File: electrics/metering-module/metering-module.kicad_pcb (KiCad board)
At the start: 2 copper layers, 86 x 31 mm, 39 parts, among them J1 North, J2 South, J3 West, J4 East, Q1 MMBT3904, Q2 MMBT3904, U1 LTV-817S, U2 LTV-817S, U3 BA033CC0FP-E2, U4 MAX3486, U5 MAX3486, U6 MCP23009-E_SS

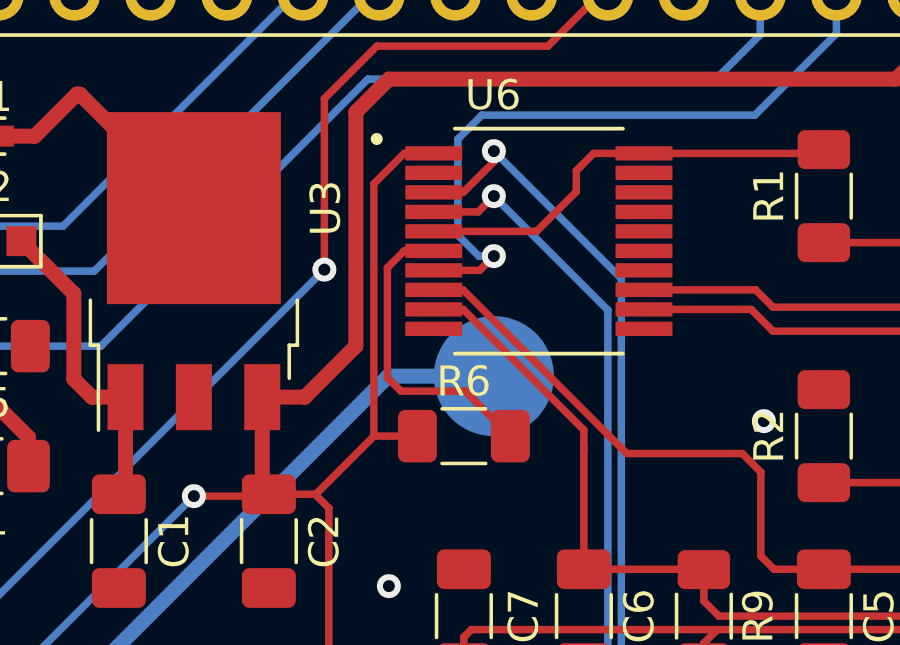
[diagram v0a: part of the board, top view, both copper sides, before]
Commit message: Added product numbers for cost calculation
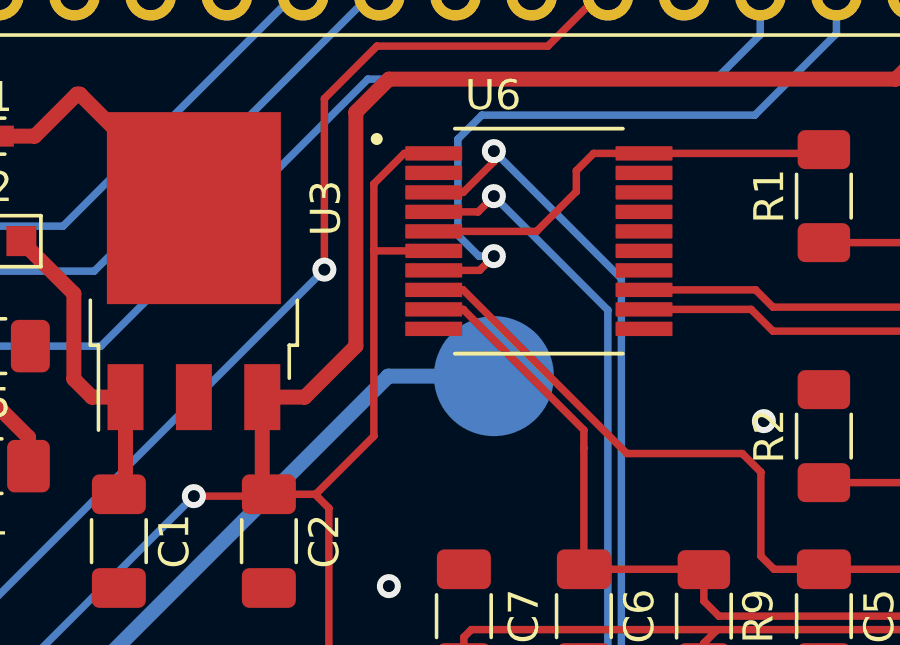
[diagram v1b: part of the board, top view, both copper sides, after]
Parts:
- removed R6: 0R, Resistor_SMD:R_1206_3216Metric_Pad1.30x1.75mm_HandSolder
- C1: value 100nF / 35V -> 100nF
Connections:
- U6 pad 6: IO_RESET -> +3V3
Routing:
- net IO_RESET: track 10.3 -> 0.00 mm
- net +3V3: track 125.6 -> 126.1 mm
